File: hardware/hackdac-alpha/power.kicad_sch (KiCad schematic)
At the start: 64 parts, among them J10 HOLE, J11 HOLE, J12 EXT POWER, J5 EXT 5V, J6 HOLE, J7 HOLE, J8 HOLE, J9 HOLE, P3 P20, P4 P28, Q6 IRLML2244, U10 KF50BDT, U11 L78L05_SO8, U12 L79L05_SO8, U13 LM66200, U14 TPS61170DRVR, U15 TPS63700DRCT, U3 TLE2082

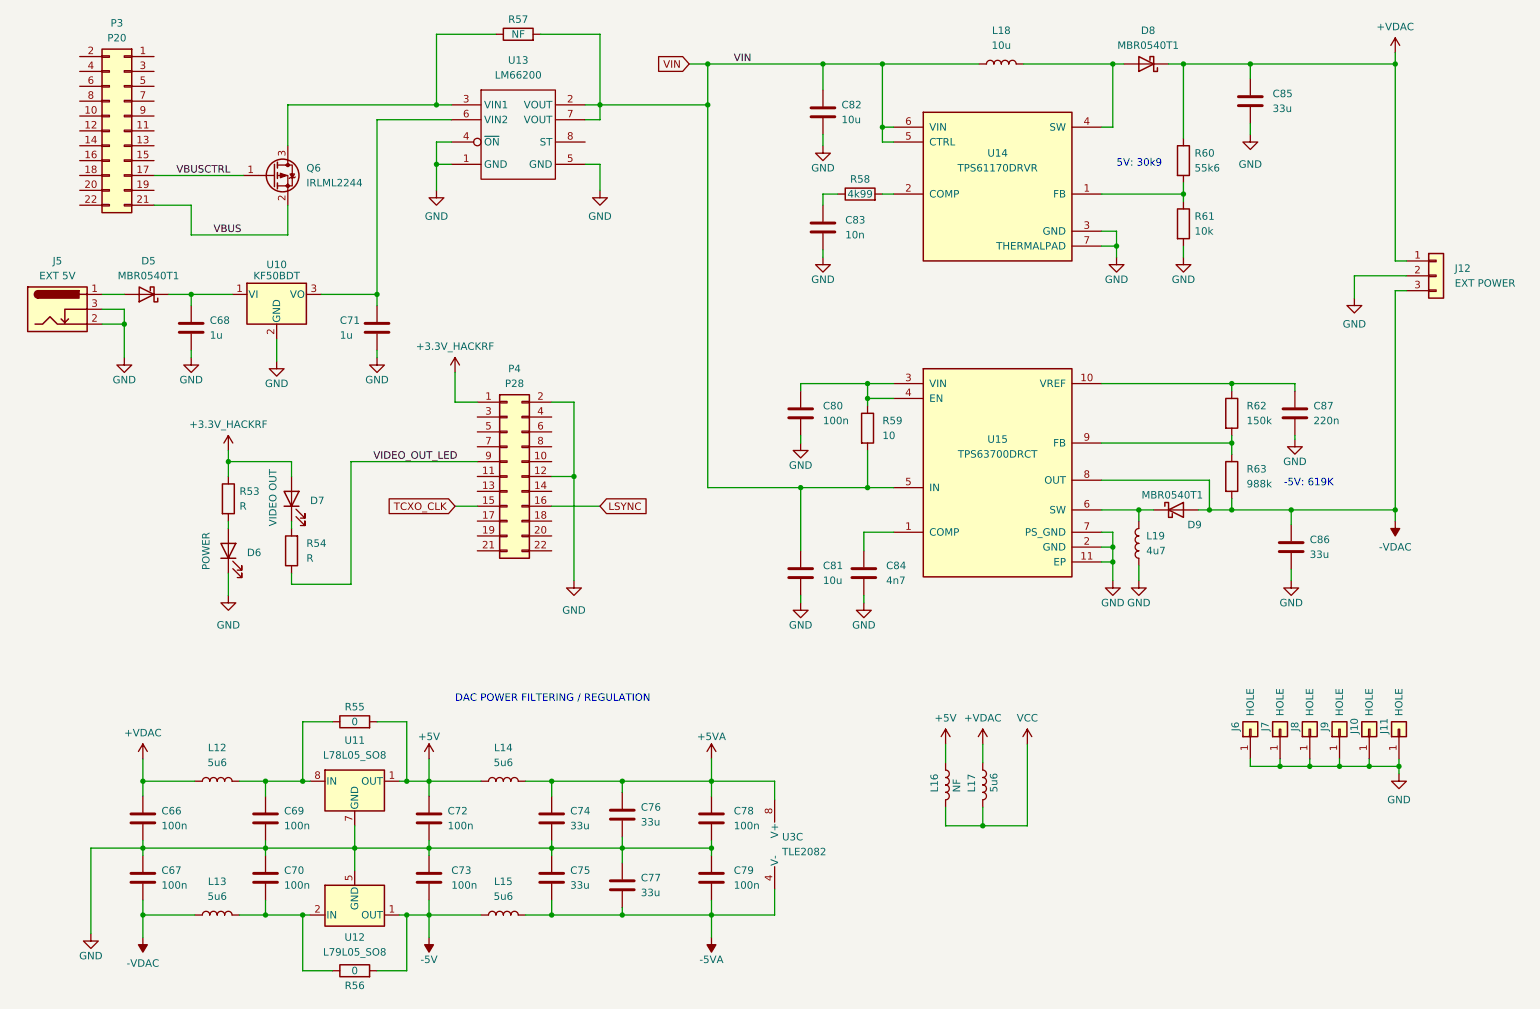
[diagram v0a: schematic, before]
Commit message: Add missing component values
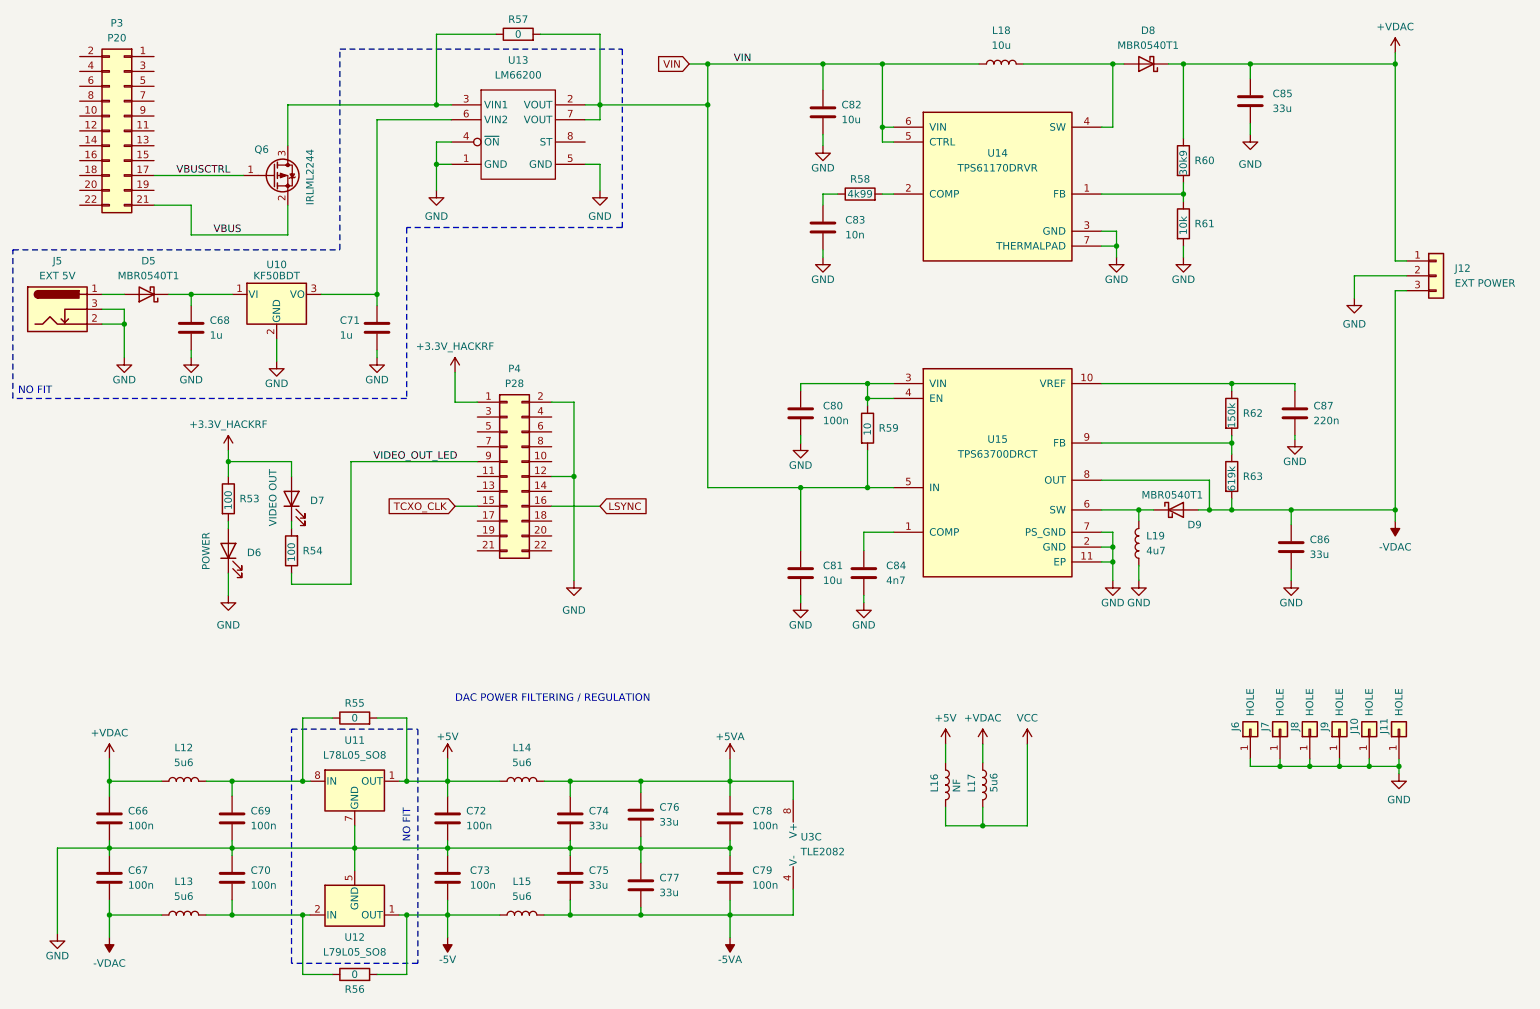
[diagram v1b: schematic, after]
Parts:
- R53, R54: value R -> 100
- R57: value NF -> 0
- R60: value 55k6 -> 30k9
- R63: value 988k -> 619k
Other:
- note added: "NO FIT"
- note removed: "-5V: 619K"
- note removed: "5V: 30k9"
- moved on the sheet: C66, C67, C69, C70, C72, C73, C74, C75, C76, C77, C78, C79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

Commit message: Update with V2 mods
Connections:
- net TCXO_ENABLE: now reaches P4.3 (Pin_3)
- net TCXO_CLK: no longer names the net of P4.15 (Pin_15)
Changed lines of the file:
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@@
-	(wire
-		(pts
-			(xy 97.79 104.14) (xy 101.6 104.14)
-		)
-		(stroke
-			(width 0)
-			(type default)
-		)
-	)
 	(wire
 		(pts
@@
 		(pts
 			(xy 122.555 38.1) (xy 122.555 35.56)
+		)
+		(stroke
+			(width 0)
+			(type default)
+		)
+	)
+	(wire
+		(pts
+			(xy 97.79 88.9) (xy 101.6 88.9)
 		)
 		(stroke
@@
 			)
 			(justify left bottom)
-		)
-	)
-	(global_label "TCXO_CLK"
-		(shape input)
-		(at 97.79 104.14 180)
-		(fields_autoplaced yes)
-		(effects
-			(font
-				(size 1.27 1.27)
-			)
-			(justify right)
-		)
-		(property "Intersheetrefs" "${INTERSHEET_REFS}"
-			(at 85.4915 104.14 0)
-			(effects
-				(font
-					(size 1.27 1.27)
-				)
-				(justify right)
-				(hide yes)
-			)
 		)
 	)
@@
 				(hide yes)
 			)
+		)
+	)
+	(global_label "TCXO_ENABLE"
+		(shape input)
+		(at 97.79 88.9 180)
+		(fields_autoplaced yes)
+		(effects
+			(font
+				(size 1.27 1.27)
+			)
+			(justify right)
+		)
+		(property "Intersheetrefs" "${INTERSHEET_REFS}"
+			(at 82.0444 88.9 0)
+			(effects
+				(font
+					(size 1.27 1.27)
+				)
+				(justify right)
+				(hide yes)
+			)

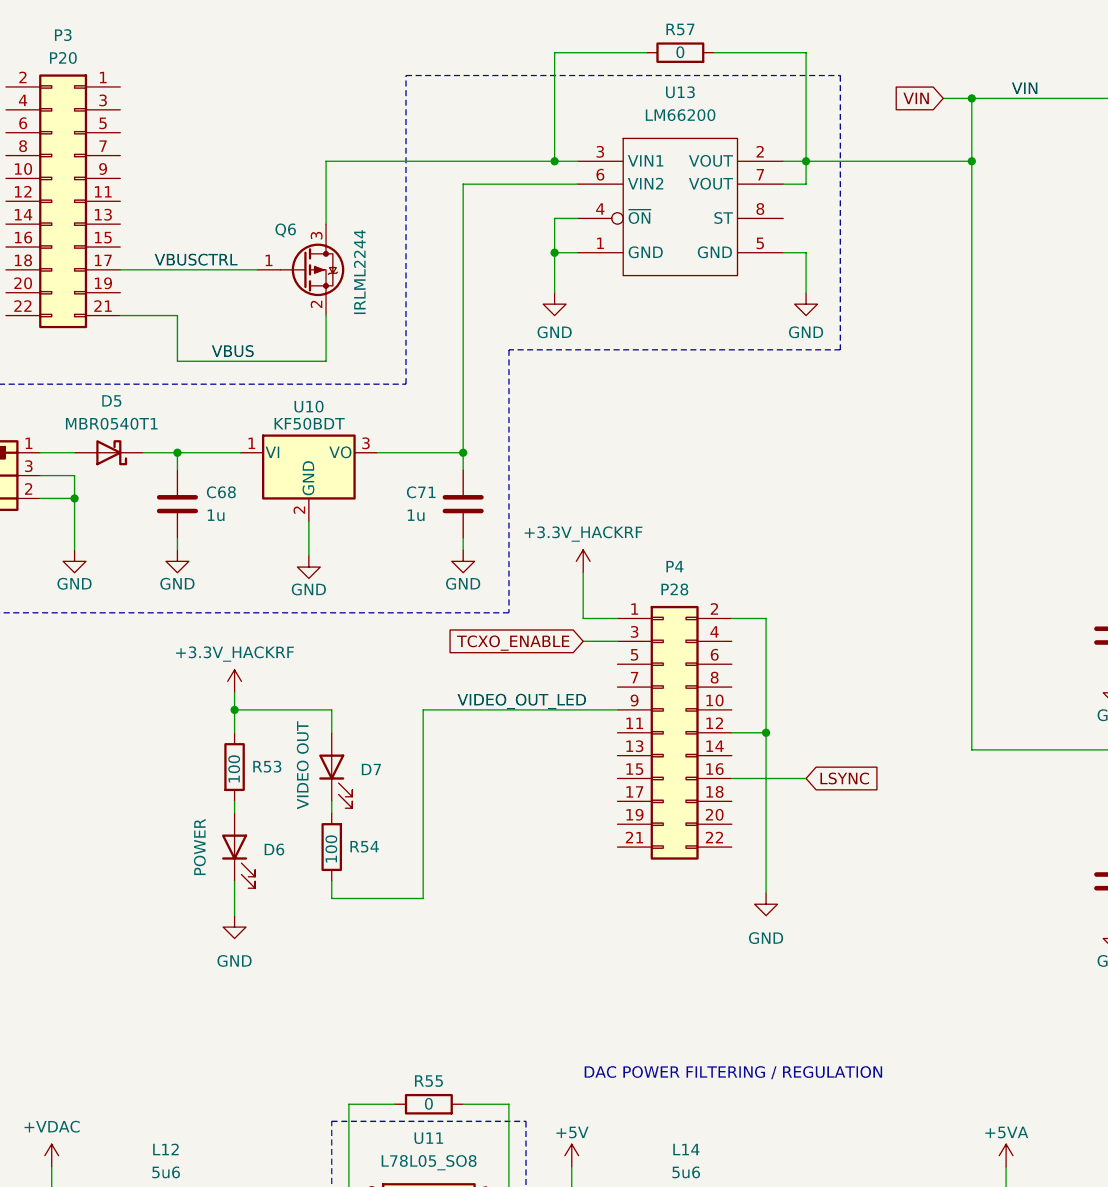
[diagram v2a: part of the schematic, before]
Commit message: Final values for V2 board
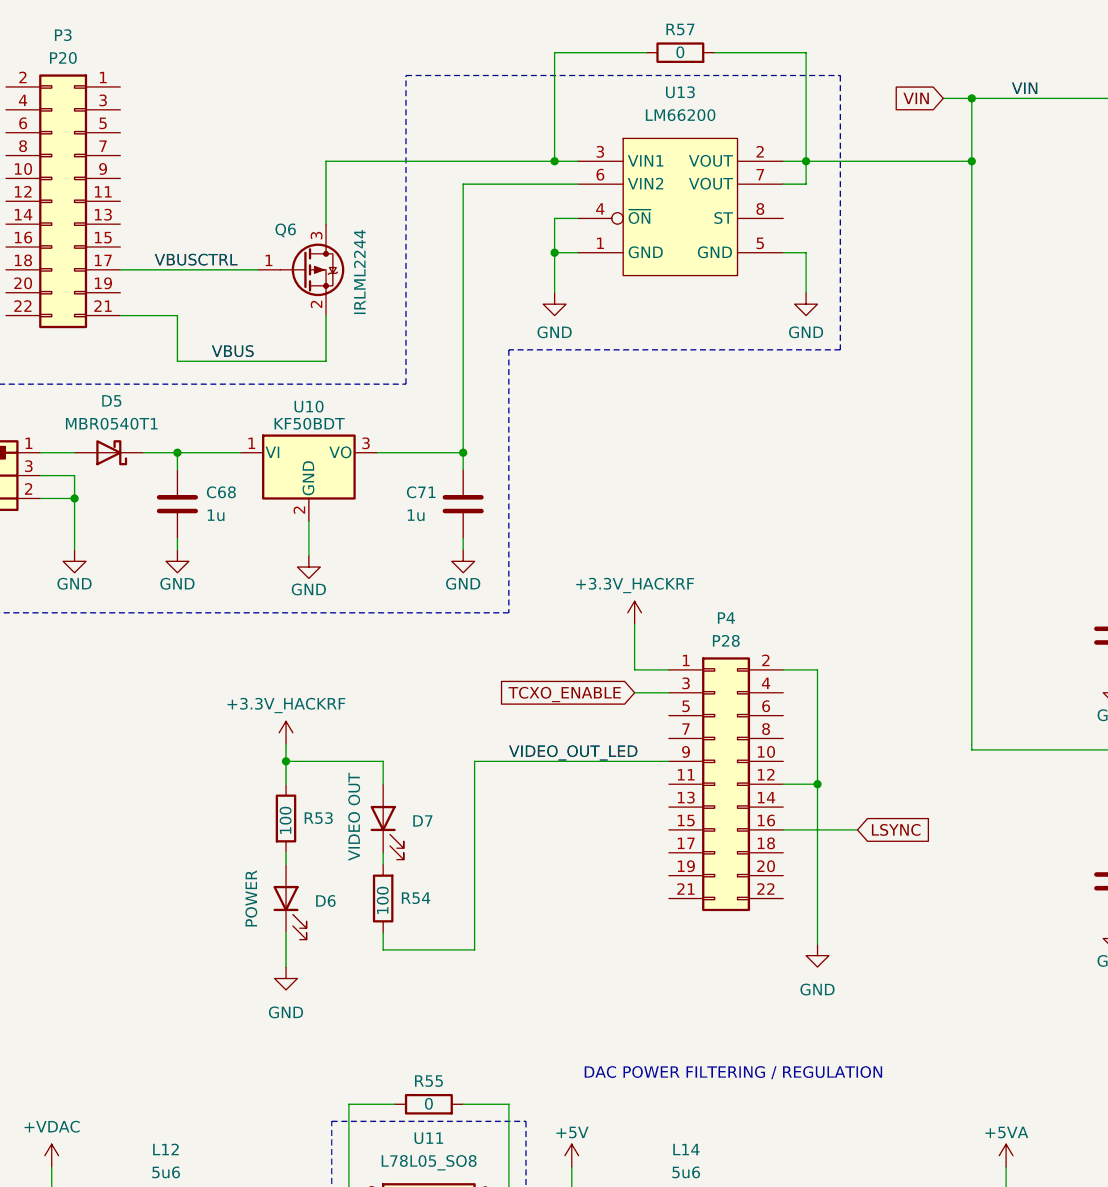
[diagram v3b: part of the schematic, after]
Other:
- moved on the sheet: D6, D7, P4, R53, R54

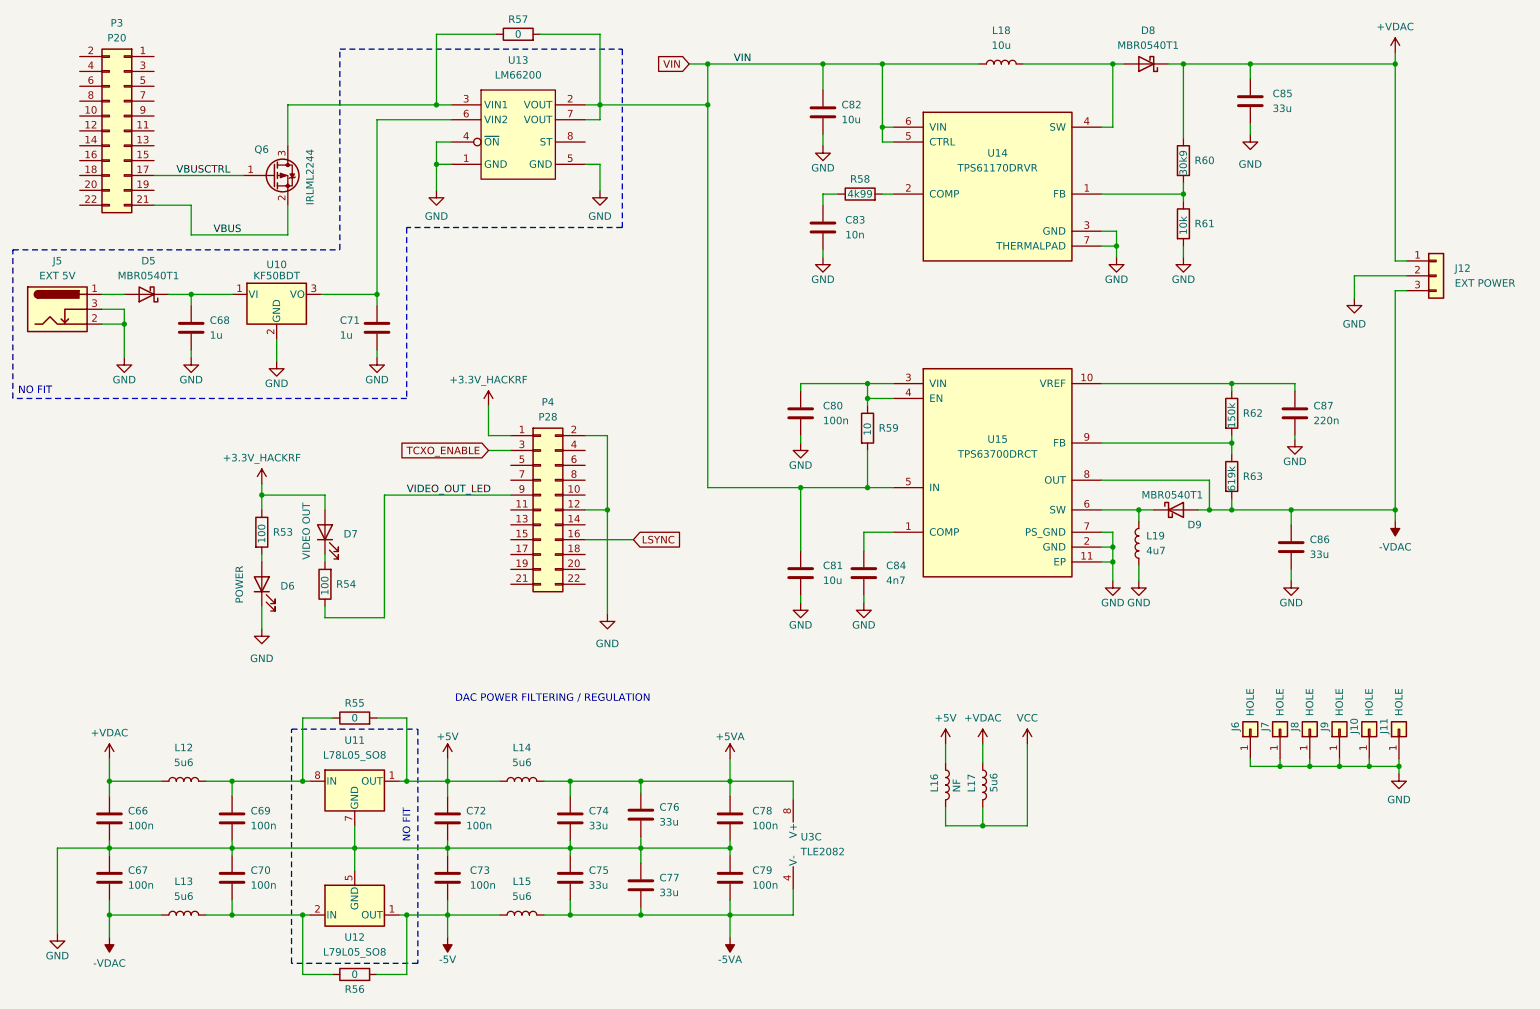
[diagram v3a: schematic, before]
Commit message: More V3 component rationalisation
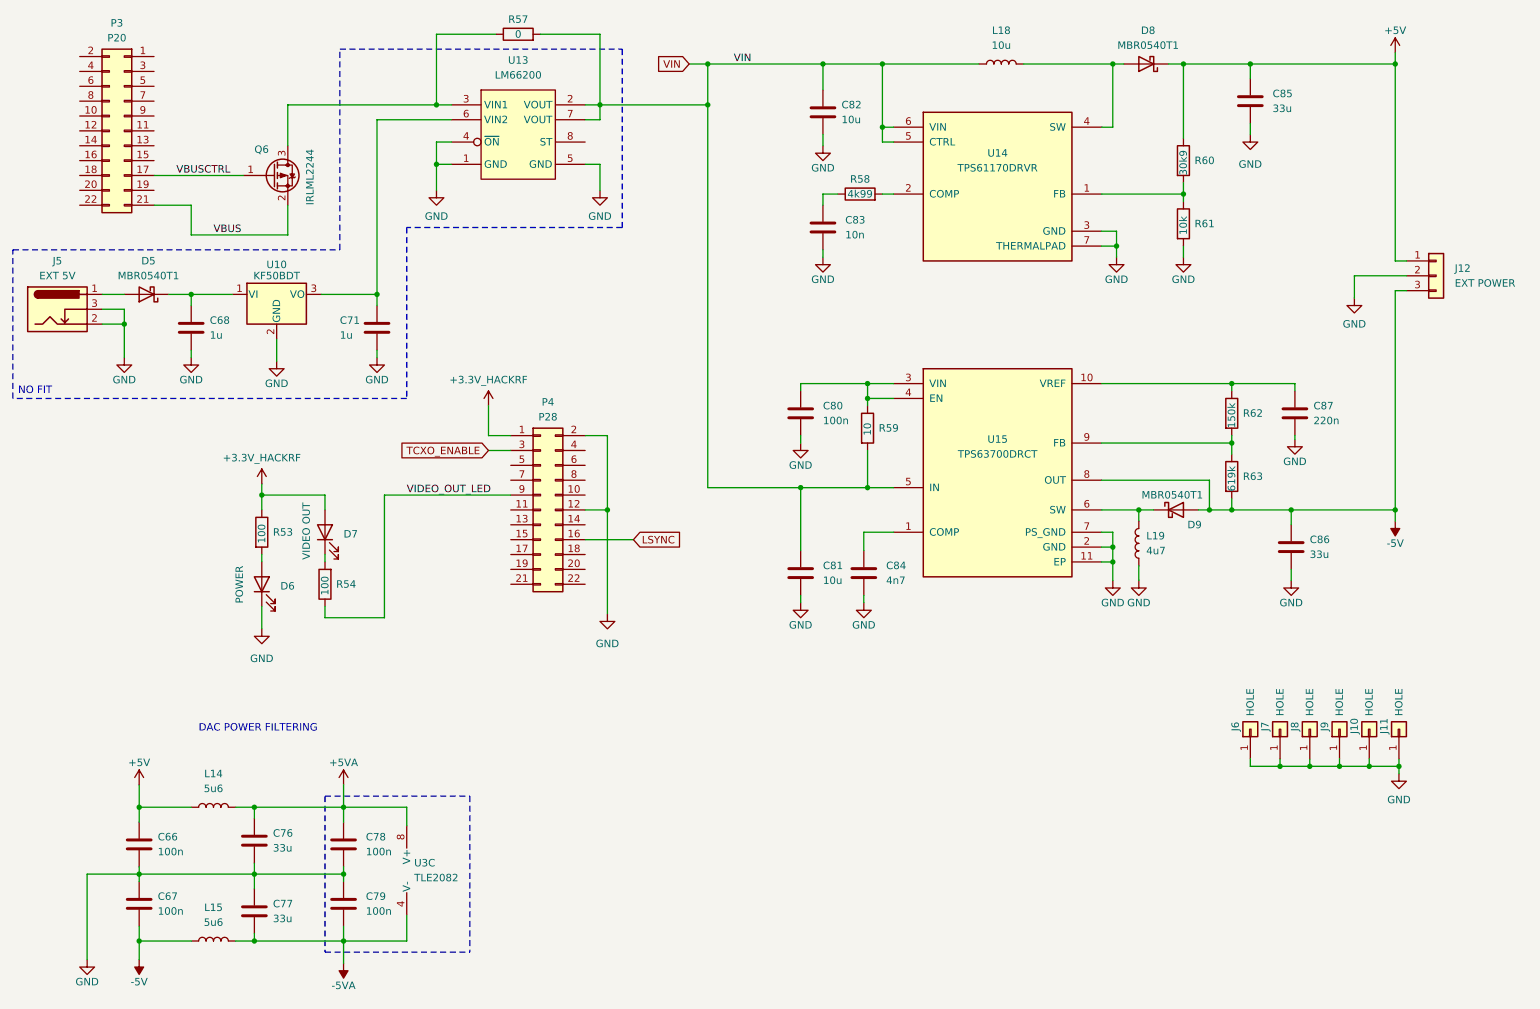
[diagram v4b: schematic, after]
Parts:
- removed C69, C70, C72, C73: 100n, Capacitor_SMD:C_0603_1608Metric, symbol Device:C
- removed C74, C75: 33u, Capacitor_SMD:C_1210_3225Metric, symbol Device:C
- removed L12, L13, L17: 5u6, Inductor_SMD:L_1210_3225Metric, symbol Device:L
- removed L16: NF, Inductor_SMD:L_1210_3225Metric, symbol Device:L
- removed R55, R56: 0, Resistor_SMD:R_0603_1608Metric, symbol Device:R
- removed U11: L78L05_SO8, Package_SO:SOIC-8_3.9x4.9mm_P1.27mm, symbol Regulator_Linear:L78L05_SO8
- removed U12: L79L05_SO8, Package_SO:SOIC-8_3.9x4.9mm_P1.27mm, symbol Regulator_Linear:L79L05_SO8
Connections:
- net +VDAC is gone; now on net +5V: C66.1, C85.1, D8.1 (K), J12.1 (Pin_1), R60.1
- net -VDAC is gone; now on net -5V: C67.2, C86.1, D9.2 (A), J12.3 (Pin_3), R63.2, U15.8 (OUT)
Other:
- note added: "DAC POWER FILTERING"
- note removed: "DAC POWER FILTERING / REGULATION"
- moved on the sheet: C66, C67, C76, C77, C78, C79, L14, L15, U3C

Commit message: Last of major V3 changes
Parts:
- removed C68, C71: 1u, Capacitor_SMD:C_0603_1608Metric, symbol Device:C
- removed D5: MBR0540T1, Diode_SMD:D_SOD-123, symbol Device:D_Schottky
- removed J5: EXT 5V, Connector_BarrelJack:BarrelJack_Horizontal, symbol Connector:Barrel_Jack_Switch
- removed R57: 0, Resistor_SMD:R_0603_1608Metric, symbol Device:R
- removed U10: KF50BDT, Package_TO_SOT_SMD:TO-252-2, symbol Regulator_Linear:KF33BDT
- removed U13: LM66200, Package_TO_SOT_SMD:SOT-583-8, symbol LM66200:LM66200
- added D5: RF OUT, LED_SMD:LED_0805_2012Metric, symbol Device:LED
- added J5: EXT LEDS, symbol Connector_Generic:Conn_01x04
- added R45: 10k, symbol Device:R
- added R46: 100, Resistor_SMD:R_0603_1608Metric, symbol Device:R
- added R47, R48, R49: 100, symbol Device:R
- added U7: 74LVC1G07, symbol 74xGxx:74LVC1G07
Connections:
- net +3.3V_HACKRF: now also D6.2 (A), D5.2 (A), J5.1 (Pin_1), U7.5 (VCC); no longer R53.1
- net GND: now also P3.13 (Pin_13), P3.15 (Pin_15), P3.19 (Pin_19), R53.2, R47.1, U7.3 (GND); no longer D6.1 (K)
- net VBUS: now also R45.2
- net VIDEO_OUT_LED: now also R46.1, R48.1; no longer R54.1
- net VIN: now also Q6.3 (D)
- net at D7.1 (K): now also R46.2; no longer R54.2
- net RF_OUT_LED: now reaches P4.7 (Pin_7)
- net RF_OUT_LED: now also R54.1, R49.1
- net VBUSCTRL: no longer names the net of Q6.1 (G)
- net VBUSCTRL: now also R45.1, U7.4; no longer P3.17 (Pin_17)
- new net: J5.2 (Pin_2), R47.2
- new net: D6.1 (K), R53.1
- new net: J5.3 (Pin_3), R48.2
- new net: J5.4 (Pin_4), R49.2
- new net: D5.1 (K), R54.2
- new net PWR_EN: U7.2
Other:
- moved on the sheet: C66, C67, C76, C77, C78, C79, C80, C81, C82, C83, C84, C85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
